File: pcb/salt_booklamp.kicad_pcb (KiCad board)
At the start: 2 copper layers, 45.1 x 45.1 mm, 33 parts, among them J1 USB-C31-S-RA-CS1E-BK-T/R, P1 PIC-TC2050-IDC, U1 PIC16F15213T-I/MF, U2 BQ21040DBVR, U3 TPS61158DRVR

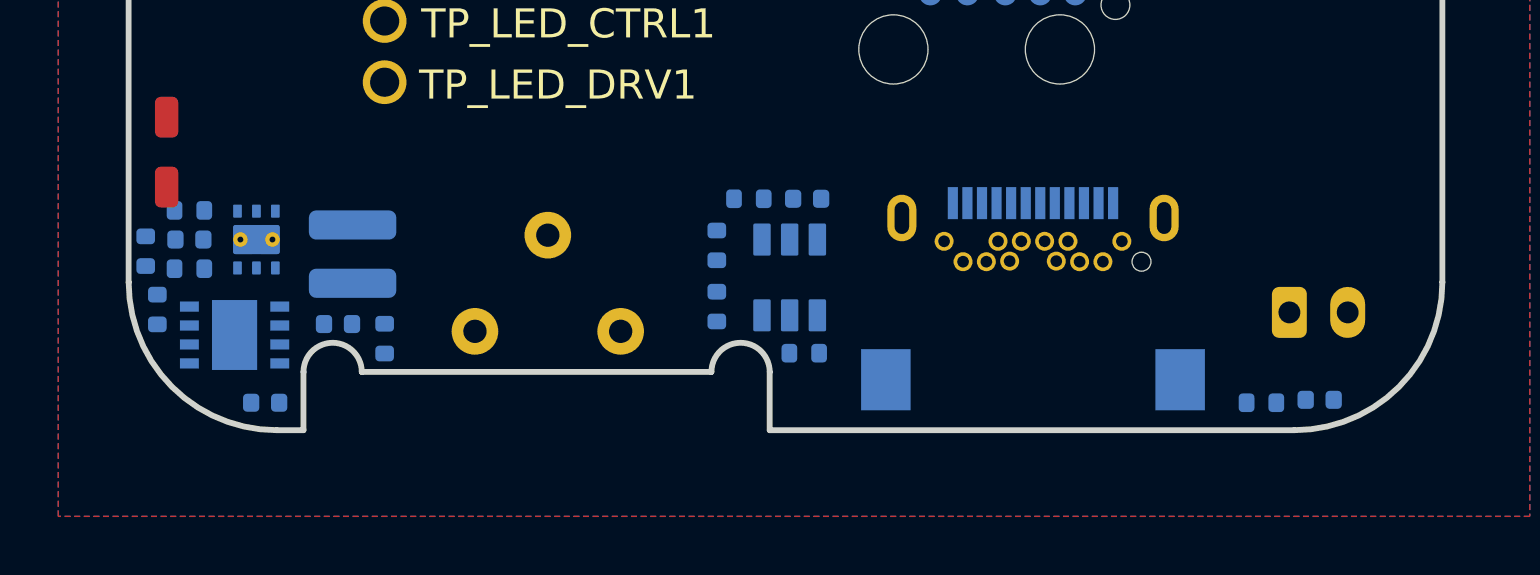
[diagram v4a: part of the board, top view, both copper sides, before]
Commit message: adjust placement of edge components in PCA, added lanyard hole in wood enclosure, updated light guide .dxf file, updated mirror film .dxf file, exported wood enclosure .step for quote, exported light guide .dxf for quote, exported switch cover for quote, imported new PCA placement, need to update switch cover, need to consider tape/sticker for pca/lgp subassembly
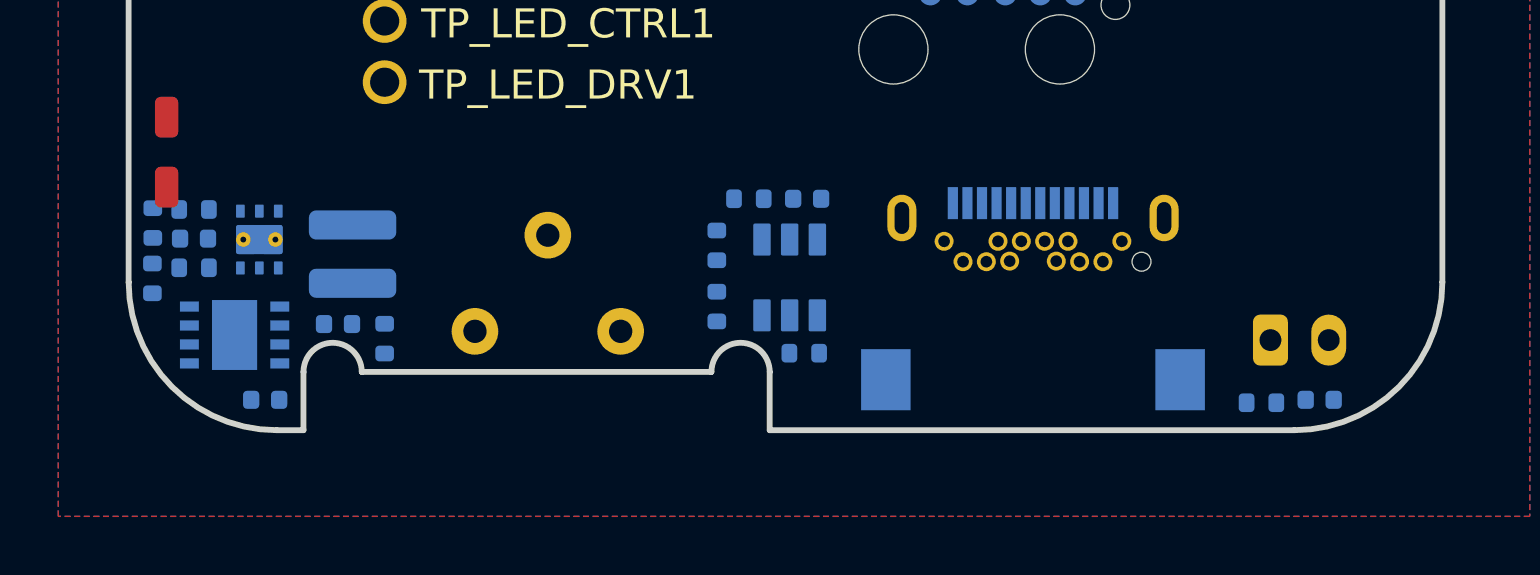
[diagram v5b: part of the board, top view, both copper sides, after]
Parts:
- moved BATT1 1.15 mm to (240.9, 148.5)
- moved R3 1.08 mm to (202.5, 146.4)
- moved R8 1.00 mm to (202.5, 144.5)
- moved C4 0.16 mm to (203.9, 145.0)
- moved R2 0.16 mm to (203.9, 144.0)
- moved R4 0.16 mm to (203.9, 146.0)
- moved C3 0.10 mm to (206.4, 150.5)
- moved U3 0.10 mm to (206.2, 145.0)
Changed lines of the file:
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@@
 			(at 0 -0.5 0)
 			(unlocked yes)
-			(layer "Rescue")
+			(layer "Cmts.User")
 			(effects
 				(font
@@
 			(at 0 -0.5 0)
 			(unlocked yes)
-			(layer "Rescue")
+			(layer "Cmts.User")
 			(effects
 				(font
@@
 			(at 0 -0.5 0)
 			(unlocked yes)
-			(layer "Rescue")
+			(layer "Cmts.User")
 			(effects
 				(font
@@
 			(at 0 -0.5 0)
 			(unlocked yes)
-			(layer "Rescue")
+			(layer "Cmts.User")
 			(effects
 				(font
@@
 			(at 0 -0.5 0)
 			(unlocked yes)
-			(layer "Rescue")
+			(layer "Cmts.User")
 			(effects
 				(font
@@
 			(at 0 -0.5 0)
 			(unlocked yes)
-			(layer "Rescue")
+			(layer "Cmts.User")
 			(effects
 				(font
@@
 			(at 0 -0.5 0)
 			(unlocked yes)
-			(layer "Rescue")
+			(layer "Cmts.User")
 			(effects
 				(font
@@
 	(footprint "Resistor_SMD:R_0402_1005Metric"
 		(layer "B.Cu")
-		(at 203.782 144.032)
+		(at 203.941593 143.999812)
 		(descr "Resistor SMD 0402 (1005 Metric), square (rectangular) end terminal, IPC_7351 nominal, (Body size source: IPC-SM-782 page 72, https://www.pcb-3d.com/wordpress/wp-content/uploads/ipc-sm-782a_amendment_1_and_2.pdf), generated with kicad-footprint-generator")
 		(tags "resistor")
@@
 	(footprint "salt_booklamp_footprints:6-WDFN - TPS61158DRVR"
 		(layer "B.Cu")
-		(at 206.082 145.032 90)
+		(at 206.182 145.032 90)
 		(property "Reference" "U3"
 			(at 0 2.1 270)
@@
 	(footprint "Capacitor_SMD:C_0402_1005Metric"
 		(layer "B.Cu")
-		(at 206.382 150.632)
+		(at 206.382 150.532)
 		(descr "Capacitor SMD 0402 (1005 Metric), square (rectangular) end terminal, IPC_7351 nominal, (Body size source: IPC-SM-782 page 76, https://www.pcb-3d.com/wordpress/wp-content/uploads/ipc-sm-782a_amendment_1_and_2.pdf), generated with kicad-footprint-generator")
 		(tags "capacitor")
@@
 	(footprint "GymTimer:JST_PH_S2B-PH-K_1x02_P2.00mm_Horizontal"
 		(layer "B.Cu")
-		(at 241.532 147.532)
+		(at 240.882 148.482)
 		(descr "JST PH series connector, S2B-PH-K (http://www.jst-mfg.com/product/pdf/eng/ePH.pdf), generated with kicad-footprint-generator")
 		(tags "connector JST PH top entry")
@@
 	(footprint "Resistor_SMD:R_0402_1005Metric"
 		(layer "B.Cu")
-		(at 202.682 147.432 90)
+		(at 202.512418 146.364834 90)
 		(descr "Resistor SMD 0402 (1005 Metric), square (rectangular) end terminal, IPC_7351 nominal, (Body size source: IPC-SM-782 page 72, https://www.pcb-3d.com/wordpress/wp-content/uploads/ipc-sm-782a_amendment_1_and_2.pdf), generated with kicad-footprint-generator")
 		(tags "resistor")
@@
 	(footprint "Capacitor_SMD:C_0402_1005Metric"
 		(layer "B.Cu")
-		(at 203.782 145.032 180)
+		(at 203.941593 144.999812 180)
 		(descr "Capacitor SMD 0402 (1005 Metric), square (rectangular) end terminal, IPC_7351 nominal, (Body size source: IPC-SM-782 page 76, https://www.pcb-3d.com/wordpress/wp-content/uploads/ipc-sm-782a_amendment_1_and_2.pdf), generated with kicad-footprint-generator")
 		(tags "capacitor")
@@
 	(footprint "Resistor_SMD:R_0402_1005Metric"
 		(layer "B.Cu")
-		(at 203.782 146.032 180)
+		(at 203.941593 145.999812 180)
 		(descr "Resistor SMD 0402 (1005 Metric), square (rectangular) end terminal, IPC_7351 nominal, (Body size source: IPC-SM-782 page 72, https://www.pcb-3d.com/wordpress/wp-content/uploads/ipc-sm-782a_amendment_1_and_2.pdf), generated with kicad-footprint-generator")
 		(tags "resistor")
@@
 	(footprint "Resistor_SMD:R_0402_1005Metric"
 		(layer "B.Cu")
-		(at 202.282 145.432 90)
+		(at 202.525937 144.465367 90)
 		(descr "Resistor SMD 0402 (1005 Metric), square (rectangular) end terminal, IPC_7351 nominal, (Body size source: IPC-SM-782 page 72, https://www.pcb-3d.com/wordpress/wp-content/uploads/ipc-sm-782a_amendment_1_and_2.pdf), generated with kicad-footprint-generator")
 		(tags "resistor")

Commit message: Routing work
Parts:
- P1: moved to F.Cu
- moved TP_5V_USB1 13.4 mm to (208.1, 140.2), turned to 90 degrees
- moved TP_3.7V_BATT1 11.1 mm to (210.2, 140.2), turned to 90 degrees
- moved TP_LED_DRV1 10.2 mm to (220.7, 140.2), turned to 90 degrees
- moved TP_GND1 9.18 mm to (212.3, 140.2), turned to 90 degrees
- moved TP_LED_CTRL1 8.54 mm to (218.6, 140.2), turned to 90 degrees
- moved TP_~{SWITCH}1 7.93 mm to (214.4, 140.2), turned to 90 degrees
- moved TP_~{CHARGING}1 7.68 mm to (216.5, 140.2), turned to 90 degrees
- moved R10 5.50 mm to (224.9, 149.8), turned to 180 degrees
- moved R6 5.30 mm to (225.3, 143.7)
- moved C1 5.19 mm to (224.9, 148.8)
- moved P1 4.76 mm to (232.2, 138.0), turned to 180 degrees
- moved R1 0.26 mm to (223.2, 143.7), turned to 180 degrees
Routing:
- net +3.7_VBATT: track 0.03 -> 75.9 mm, vias 0 -> 2
- net /~{SWITCH}: track 0.00 -> 52.5 mm, vias 0 -> 3
- net /LED_DRV: track 0.00 -> 49.9 mm, vias 0 -> 2
- net +5V_USB: track 0.00 -> 40.5 mm, vias 0 -> 2
- net /LED_CTRL: track 0.00 -> 37.0 mm, vias 0 -> 3
- net Net-(P1-~{MCLR}): track 0.00 -> 36.6 mm, vias 0 -> 1
- net Net-(P1-ICSPCLK): track 0.00 -> 36.5 mm, vias 0 -> 1
- net /~{CHARGING}: track 0.00 -> 31.5 mm, vias 0 -> 3
- net Net-(P1-ICSPDAT): track 0.00 -> 28.0 mm, vias 0 -> 2
- net Net-(LED1-k): track 0.00 -> 28.0 mm, vias 0 -> 2
- net Net-(LED2-a): track 0.00 -> 19.8 mm, vias 0 -> 3
- net Net-(J1-CC1): track 0.00 -> 11.5 mm, vias 0 -> 2
- net Net-(J1-CC2): track 0.00 -> 10.6 mm, vias 0 -> 1
- net Net-(R7-Pad2): track 0.00 -> 7.03 mm, vias 0 -> 1
- net Net-(U2-ISET): track 0.00 -> 5.02 mm, vias 0 -> 2
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
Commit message: ordered pca, wood, copper, batteries
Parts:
- removed R7: 0r0, Resistor_SMD:R_0402_1005Metric
- moved P1 24.0 mm to (208.2, 137.6), turned to 0 degrees
- moved TP_5V_USB1 16.4 mm to (218.9, 127.9), turned to 0 degrees
- moved R9 15.9 mm to (224.7, 149.4), turned to -90 degrees
- moved TP_3.7V_BATT1 13.4 mm to (218.9, 130.0), turned to 0 degrees
- moved TP_GND1 10.5 mm to (218.9, 132.1), turned to 0 degrees
- moved TP_~{SWITCH}1 7.53 mm to (218.9, 134.2), turned to 0 degrees
- moved TP_~{CHARGING}1 4.61 mm to (218.9, 136.3), turned to 0 degrees
- moved C1 3.40 mm to (221.9, 147.2), turned to 90 degrees
- moved TP_LED_CTRL1 1.84 mm to (218.9, 138.4), turned to 0 degrees
- moved TP_LED_DRV1 1.78 mm to (218.9, 140.5), turned to 0 degrees
- moved R5 1.69 mm to (208.9, 147.9), turned to 0 degrees
- moved C5 1.65 mm to (210.5, 148.3), turned to -90 degrees
- moved R10 0.92 mm to (225.7, 149.4), turned to -90 degrees
- moved R2 0.72 mm to (203.5, 144.6), turned to 90 degrees
- moved C4 0.64 mm to (204.4, 144.6), turned to 90 degrees
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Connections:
- P1 pad 10: +5V_USB -> unconnected-(P1-Pad10)
- P1 pad 2: /LED_CTRL -> unconnected-(P1-Pad2)
- P1 pad 4: +3.7_VBATT -> unconnected-(P1-Pad4)
- P1 pad 6: GND -> unconnected-(P1-Pad6)
- P1 pad 8: /~{SWITCH} -> unconnected-(P1-Pad8)
- R1 pad 2: Net-(U2-TS) -> Net-(U2-ISET)
- R6 pad 1: Net-(U2-ISET) -> Net-(U2-TS)
- S1 pad 2: Net-(R7-Pad2) -> GND
- U2 pad 2: +3.7_VBATT -> +5V_USB
- U2 pad 3: /~{CHARGING} -> GND
- U2 pad 5: GND -> /~{CHARGING}
- U2 pad 6: +5V_USB -> +3.7_VBATT
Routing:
- net +3.7_VBATT: track 75.9 -> 3.62 mm, vias 2 -> 11
- net Net-(P1-ICSPCLK): track 36.5 -> 12.4 mm
- net Net-(P1-~{MCLR}): track 36.6 -> 16.8 mm
- net /~{SWITCH}: track 52.5 -> 34.0 mm, vias 3 -> 1
- net /LED_CTRL: track 37.0 -> 20.1 mm, vias 3 -> 2
- net Net-(P1-ICSPDAT): track 28.0 -> 13.2 mm, vias 2 -> 1
- net Net-(R7-Pad2): track 7.03 -> 0.00 mm, vias 1 -> 0
- net +5V_USB: track 40.5 -> 34.7 mm
- net Net-(LED2-a): track 19.8 -> 15.4 mm, vias 3 -> 2
- net /~{CHARGING}: track 31.5 -> 35.3 mm, vias 3 -> 0
- net GND: track 2.87 -> 5.53 mm
- net Net-(J1-CC2): track 10.6 -> 8.05 mm, vias 1 -> 0
- net Net-(J1-CC1): track 11.5 -> 13.5 mm, vias 2 -> 0
- net /LED_DRV: track 49.9 -> 48.2 mm, vias 2 -> 3
- net Net-(U2-TS): track 1.67 -> 3.28 mm
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- added copper zone on In2.Cu, net +3.7_VBATT
- added copper zone on F.Cu, net +5V_USB
- added copper zone on In1.Cu, net GND
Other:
- copper layers 2 -> 4
- board text added: "0.1 mm"
- board text added: "0.1000 mm / 0.1000 mm"
- board text added: "0.1500 mm"
- board text added: "0.44 mm"
- board text added: "4"
- board text added: "In1.Cu"
- board text added: "In2.Cu"
- board text added: "prepreg"
- board text removed: "0.1524 mm / 0.1270 mm"
- board text removed: "0.2540 mm"
- board text removed: "0.71 mm"
- board text removed: "2"

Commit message: build7 fixes - interposer for pcb error, new switch retainer, new mirror film, adhesive film to test
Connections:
- R1 pad 2: Net-(U2-ISET) -> Net-(U2-TS)
- R6 pad 1: Net-(U2-TS) -> Net-(U2-ISET)
- U2 pad 2: +5V_USB -> +3.7_VBATT
- U2 pad 3: GND -> /~{CHARGING}
- U2 pad 5: /~{CHARGING} -> GND
- U2 pad 6: +3.7_VBATT -> +5V_USB
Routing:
- net GND: vias 17 -> 16
- net /~{CHARGING}: vias 0 -> 1
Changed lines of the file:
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@@
 			)
 		)
-		(property "Description" "RES SMD 1.2K OHM 1% 1/10W 0402"
+		(property "Description" "RES SMD 5.1K OHM 0.1% 1/16W 0402"
 			(at 0 0 90)
 			(unlocked yes)
@@
 			)
 		)
-		(property "Manufacturer Part Number" "CR0603-FX-1201ELF"
+		(property "Manufacturer Part Number" "ERA-2AEB512X"
 			(at 0 0 90)
 			(unlocked yes)
@@
 			)
 		)
-		(property "Manufacturer Part Number" "RMCF0603FT6R80"
+		(property "Manufacturer Part Number" "CRCW04026R80FKED"
 			(at 0 0 90)
 			(unlocked yes)
@@
 			(layers "B.Cu" "B.Mask" "B.Paste")
 			(roundrect_rratio 0.08333333333)
-			(net 11 "+5V_USB")
+			(net 1 "+3.7_VBATT")
 			(pinfunction "VOUT")
 			(pintype "passive")
@@
 			(layers "B.Cu" "B.Mask" "B.Paste")
 			(roundrect_rratio 0.08333333333)
-			(net 14 "GND")
+			(net 29 "/~{CHARGING}")
 			(pinfunction "~{CHG}")
 			(pintype "passive")
@@
 			(layers "B.Cu" "B.Mask" "B.Paste")
 			(roundrect_rratio 0.08333333333)
-			(net 29 "/~{CHARGING}")
+			(net 14 "GND")
 			(pinfunction "GND")
 			(pintype "passive")
@@
 			(layers "B.Cu" "B.Mask" "B.Paste")
 			(roundrect_rratio 0.08333333333)
-			(net 1 "+3.7_VBATT")
+			(net 11 "+5V_USB")
 			(pinfunction "VIN")
 			(pintype "passive")
@@
 			)
 		)
-		(property "Manufacturer Part Number" "RMCF0603FT10K0"
+		(property "Manufacturer Part Number" "RC0402JR-0710KL"
 			(at 0 0 0)
 			(unlocked yes)
@@
 			(layers "B.Cu" "B.Mask" "B.Paste")
 			(roundrect_rratio 0.25)
-			(net 10 "Net-(U2-TS)")
+			(net 38 "Net-(U2-ISET)")
 			(pinfunction "1")
 			(pintype "input")
@@
 			)
 		)
-		(property "Description" "RES SMD 1.2K OHM 1% 1/10W 0402"
+		(property "Description" "RES SMD 5.1K OHM 0.1% 1/16W 0402"
 			(at 0 0 90)
 			(unlocked yes)
@@
 			)
 		)
-		(property "Manufacturer Part Number" "CR0603-FX-1201ELF"
+		(property "Manufacturer Part Number" "ERA-2AEB512X"
 			(at 0 0 90)
 			(unlocked yes)
@@
 			)
 		)
-		(property "Manufacturer Part Number" "RMCF0603FT10K0"
+		(property "Manufacturer Part Number" "RC0402JR-0710KL"
 			(at 0 0 90)
 			(unlocked yes)
@@
 			)
 		)
-		(property "Manufacturer Part Number" "RMCF0603FT10K0"
+		(property "Manufacturer Part Number" "RC0402JR-0710KL"
 			(at 0 0 180)
 			(unlocked yes)
@@
 			(layers "B.Cu" "B.Mask" "B.Paste")
 			(roundrect_rratio 0.25)
-			(net 38 "Net-(U2-ISET)")
+			(net 10 "Net-(U2-TS)")
 			(pinfunction "2")
 			(pintype "output")
@@
 			)
 		)
-		(property "Manufacturer Part Number" "RMCF0603FT10K0"
+		(property "Manufacturer Part Number" "RC0402JR-0710KL"
 			(at 0 0 180)
 			(unlocked yes)
@@
 			)
 		)
-		(property "Manufacturer Part Number" "RC0603JR-070RL"
+		(property "Manufacturer Part Number" "CRCW04020000Z0ED"
 			(at 0 0 270)
 			(unlocked yes)
@@
 		(sheetname "/")
 		(sheetfile "salt_booklamp.kicad_sch")
-		(attr smd dnp)
+		(attr smd exclude_from_bom dnp)
 		(fp_line
 			(start -0.153641 -0.38)
@@
 	)
 	(via
-		(at 209.382 146.532)
+		(at 224.382 145.032)
 		(size 0.5)
 		(drill 0.2)
@@
 	)
 	(via
-		(at 203.431593 145.999812)
+		(at 209.382 146.532)
 		(size 0.5)
 		(drill 0.2)
@@
 	)
 	(via
-		(at 205.902 150.532)
+		(at 203.431593 145.999812)
 		(size 0.5)
 		(drill 0.2)
@@
 	)
 	(via
-		(at 223.432 147.632)
+		(at 205.902 150.532)
 		(size 0.5)
 		(drill 0.2)
@@
 	)
 	(segment
+		(start 224.382 145.032)
+		(end 224.382 145.293)
+		(width 0.1)
+		(layer "B.Cu")
+		(net 1)
+	)
+	(segment
 		(start 206.182 146.007)
 		(end 206.182 146.232)
@@
 	)
 	(via
-		(at 224.382 145.032)
+		(at 221.925 147.655)
 		(size 0.5)
 		(drill 0.2)
@@
 	)
 	(via
-		(at 221.925 147.655)
+		(at 223.432 147.632)
 		(size 0.5)
 		(drill 0.2)
@@
 	)
 	(segment
-		(start 224.382 145.032)
-		(end 224.382 145.293)
-		(width 0.1)
-		(layer "B.Cu")
-		(net 11)
-	)
-	(segment
 		(start 233.982 142.912071)
 		(end 233.659965 142.590035)
@@
 		(net 14)
 	)
-	(via
-		(at 225.332 145.032)
-		(size 0.5)
-		(drill 0.2)
-		(layers "F.Cu" "B.Cu")
-		(net 14)
-	)
 	(segment
 		(start 235.482 143.782)
@@
 		(net 28)
 	)
+	(via
+		(at 225.332 145.032)
+		(size 0.5)
+		(drill 0.2)
+		(layers "F.Cu" "B.Cu")
+		(net 29)
+	)
 	(segment
